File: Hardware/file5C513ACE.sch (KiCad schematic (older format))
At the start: 73 parts, among them J1 GATE_2, J2 GATE_3, J3 GATE_1, Q1 MMBT3904, Q2 MMBT3904, Q3 MMBT3904, SW1 Frequency Adjust, SW10 SET_SW, SW11 FILTER_SW, SW12 FILTEREXT_SW, SW13 SHAPE_SW, SW2 MOD_SW, SW3 FILTER1_SW, SW4 PROG, SW5 VOICE_SW, SW6 FILTER2_SW, SW7 RST, SW8 MODE_SW, SW9 FILTER3_SW, U1 TLC5947DAP

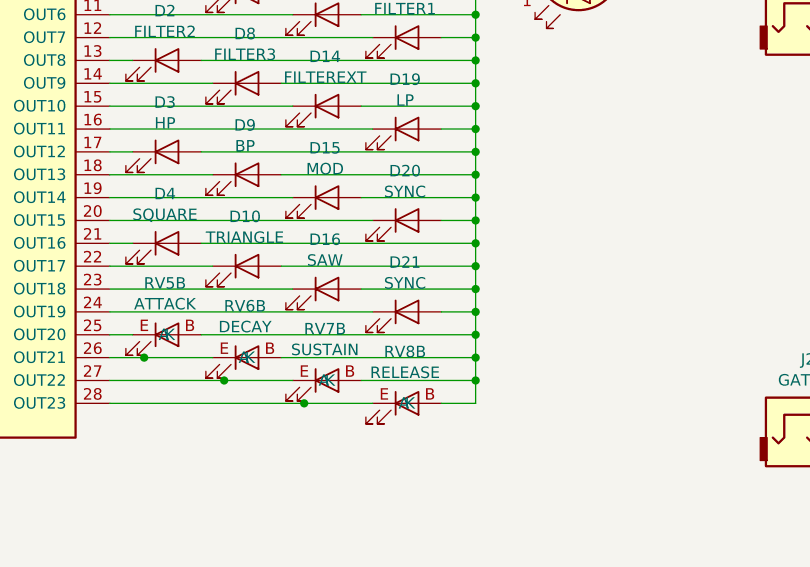
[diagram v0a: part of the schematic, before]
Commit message: Finished mechanical design on PCB
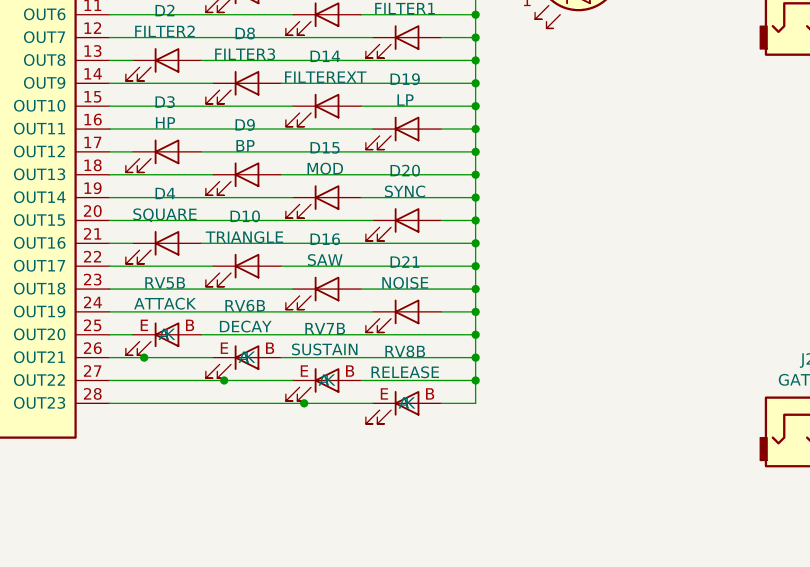
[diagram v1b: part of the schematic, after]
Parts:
- D21: value SYNC -> NOISE
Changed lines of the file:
@@
 AR Path="/5BFD63E3/5C513ACF/5C6023CE" Ref="D21"  Part="1"
 F 0 "D21" H 3791 5666 50  0000 C CNN
-F 1 "SYNC" H 3791 5575 50  0000 C CNN
+F 1 "NOISE" H 3791 5575 50  0000 C CNN
 F 2 "LED_THT:LED_D3.0mm" H 3800 5450 50  0001 C CNN
 F 3 "~" H 3800 5450 50  0001 C CNN

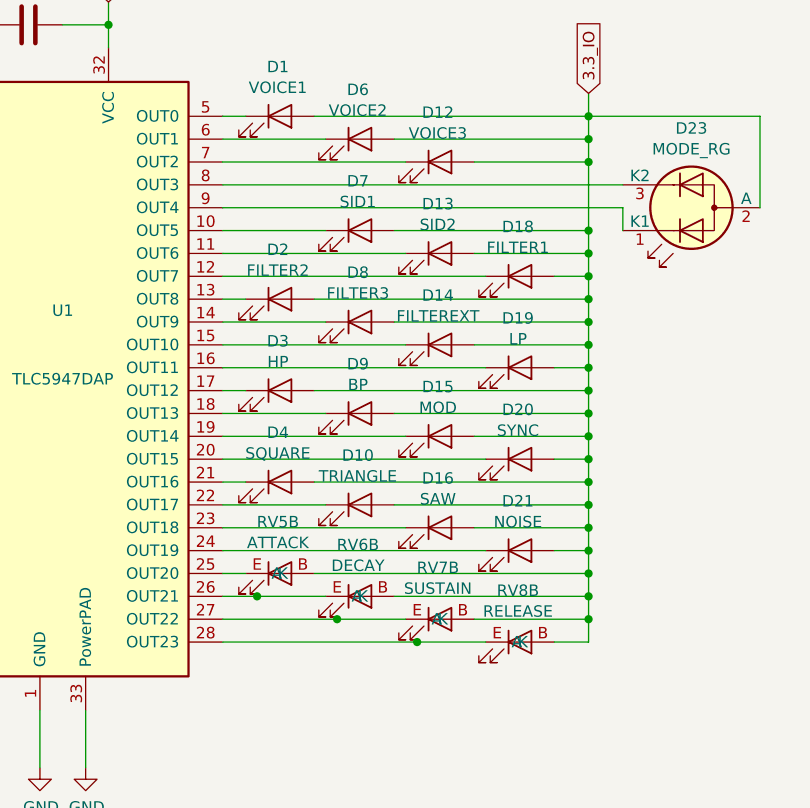
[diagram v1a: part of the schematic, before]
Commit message: Removed SID1 and SID2 led
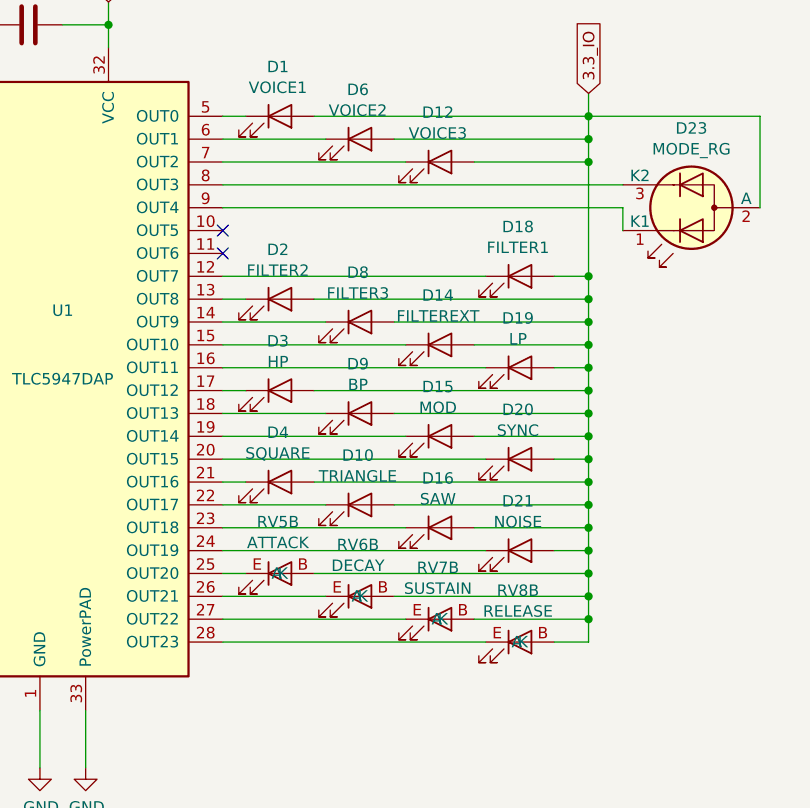
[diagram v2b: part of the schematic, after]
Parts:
- removed D13: SID2, LED_THT:LED_D3.0mm, symbol Device:LED
- removed D7: SID1, LED_THT:LED_D3.0mm, symbol Device:LED
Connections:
- no-connect marks 1 -> 3
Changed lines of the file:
@@
-$Comp
-L Device:LED D?
-U 1 1 5C602358
-P 3100 4050
-AR Path="/5BFD63E3/5C602358" Ref="D?"  Part="1"
-AR Path="/5BFD63E3/5C513ACF/5C602358" Ref="D7"  Part="1"
-F 0 "D7" H 3091 4266 50  0000 C CNN
-F 1 "SID1" H 3091 4175 50  0000 C CNN
-F 2 "LED_THT:LED_D3.0mm" H 3100 4050 50  0001 C CNN
-F 3 "~" H 3100 4050 50  0001 C CNN
-	1    3100 4050
-	1    0    0    -1
-$EndComp
-$Comp
-L Device:LED D?
-U 1 1 5C60235F
-P 3450 4150
-AR Path="/5BFD63E3/5C60235F" Ref="D?"  Part="1"
-AR Path="/5BFD63E3/5C513ACF/5C60235F" Ref="D13"  Part="1"
-F 0 "D13" H 3441 4366 50  0000 C CNN
-F 1 "SID2" H 3441 4275 50  0000 C CNN
-F 2 "LED_THT:LED_D3.0mm" H 3450 4150 50  0001 C CNN
-F 3 "~" H 3450 4150 50  0001 C CNN
-	1    3450 4150
-	1    0    0    -1
-$EndComp
 $Comp
 L Device:LED D?
@@
 	2500 3750 3300 3750
 Wire Wire Line
-	2500 4050 2950 4050
-Wire Wire Line
-	2500 4150 3300 4150
-Wire Wire Line
 	2500 4250 3650 4250
 Wire Wire Line
@@
 	2500 5550 2600 5550
 Wire Wire Line
-	2500 5650 2650 5650
-Wire Wire Line
-	2500 5750 3000 5750
-Wire Wire Line
-	2500 5850 3350 5850
-Wire Wire Line
 	4100 3450 4100 3550
 Wire Wire Line
@@
 Wire Wire Line
 	4100 4250 4100 4350
-Wire Wire Line
-	3600 4150 4100 4150
-Connection ~ 4100 4150
-Wire Wire Line
-	4100 4150 4100 4250
-Wire Wire Line
-	3250 4050 4100 4050
-Connection ~ 4100 4050
-Wire Wire Line
-	4100 4050 4100 4150
 Wire Wire Line
 	3600 3750 4100 3750
@@
 	700  4550 1100 4550
 NoConn ~ 1100 4950
-Wire Wire Line
-	4100 3750 4100 4050
 $Comp
 L Device:LED_Dual_CAC D23
@@
 	0    1    1    0
 $EndComp
-Connection ~ 2650 5650
-Wire Wire Line
-	2650 5650 2950 5650
-Connection ~ 3000 5750
-Wire Wire Line
-	3000 5750 3300 5750
-Connection ~ 3350 5850
-Wire Wire Line
-	3350 5850 3650 5850
+Wire Wire Line
+	2500 5650 2950 5650
+Wire Wire Line
+	2500 5750 3300 5750
+Wire Wire Line
+	2500 5850 3650 5850
+Wire Wire Line
+	4100 3750 4100 4250
+NoConn ~ 2500 4050
+NoConn ~ 2500 4150
 $EndSCHEMATC

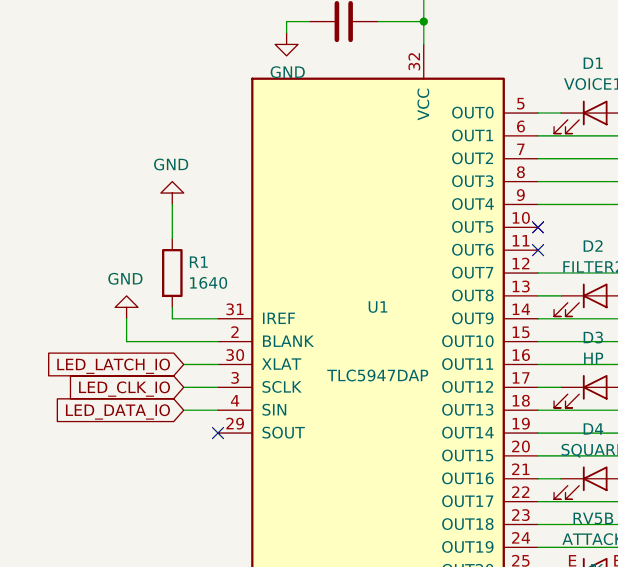
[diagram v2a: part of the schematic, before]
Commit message: STM32CubeMX Blinky
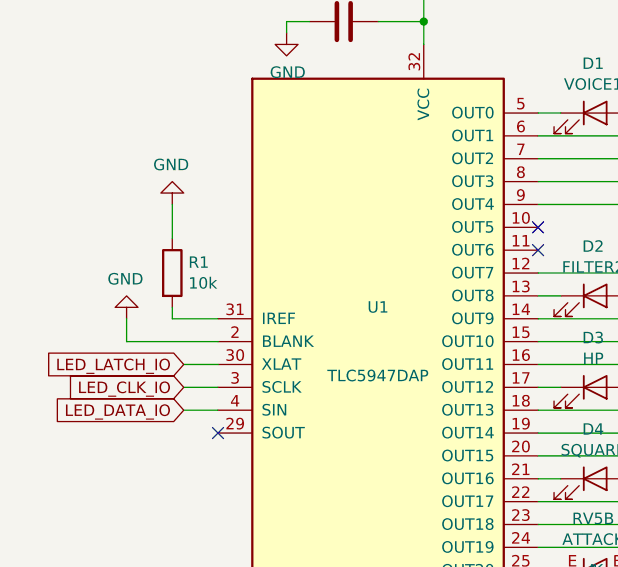
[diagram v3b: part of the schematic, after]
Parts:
- R1: value 1640 -> 10k
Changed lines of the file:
@@
 AR Path="/5BFD63E3/5C513ACF/5C602325" Ref="R1"  Part="1"
 F 0 "R1" H 970 4296 50  0000 L CNN
-F 1 "1640" H 970 4205 50  0000 L CNN
+F 1 "10k" H 970 4205 50  0000 L CNN
 F 2 "Resistor_SMD:R_0603_1608Metric" V 830 4250 50  0001 C CNN
 F 3 "~" H 900 4250 50  0001 C CNN

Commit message: IT WORKS
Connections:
- net 3.3_IO: now also C3.1, U1.32 (VCC); no longer D1.2 (A), D10.2 (A), D12.2 (A), D14.2 (A), D15.2 (A), D16.2 (A), D18.2 (A), D19.2 (A), D2.2 (A), D20.2 (A), D21.2 (A), D23.2 (A), D3.2 (A), D4.2 (A), D6.2 (A), D8.2 (A), D9.2 (A), RV5.B (A), RV6.B (A), RV7.B (A), RV8.B (A)
- net 5V_IO: now also D1.2 (A), D10.2 (A), D12.2 (A), D14.2 (A), D15.2 (A), D16.2 (A), D18.2 (A), D19.2 (A), D2.2 (A), D20.2 (A), D21.2 (A), D23.2 (A), D3.2 (A), D4.2 (A), D6.2 (A), D8.2 (A), D9.2 (A), RV5.B (A), RV6.B (A), RV7.B (A), RV8.B (A); no longer C3.1, U1.32 (VCC)
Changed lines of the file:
@@
 Text GLabel 1750 2500 3    50   Input ~ 0
 3.3_IO
-Text GLabel 2000 3050 1    50   Input ~ 0
+Text GLabel 4100 3450 1    50   Input ~ 0
 5V_IO
 Text GLabel 7250 800  1    50   Input ~ 0
@@
 	1    0    0    -1
 $EndComp
-Text GLabel 4100 3450 1    50   Input ~ 0
+Text GLabel 2000 3050 1    50   Input ~ 0
 3.3_IO
 $Comp

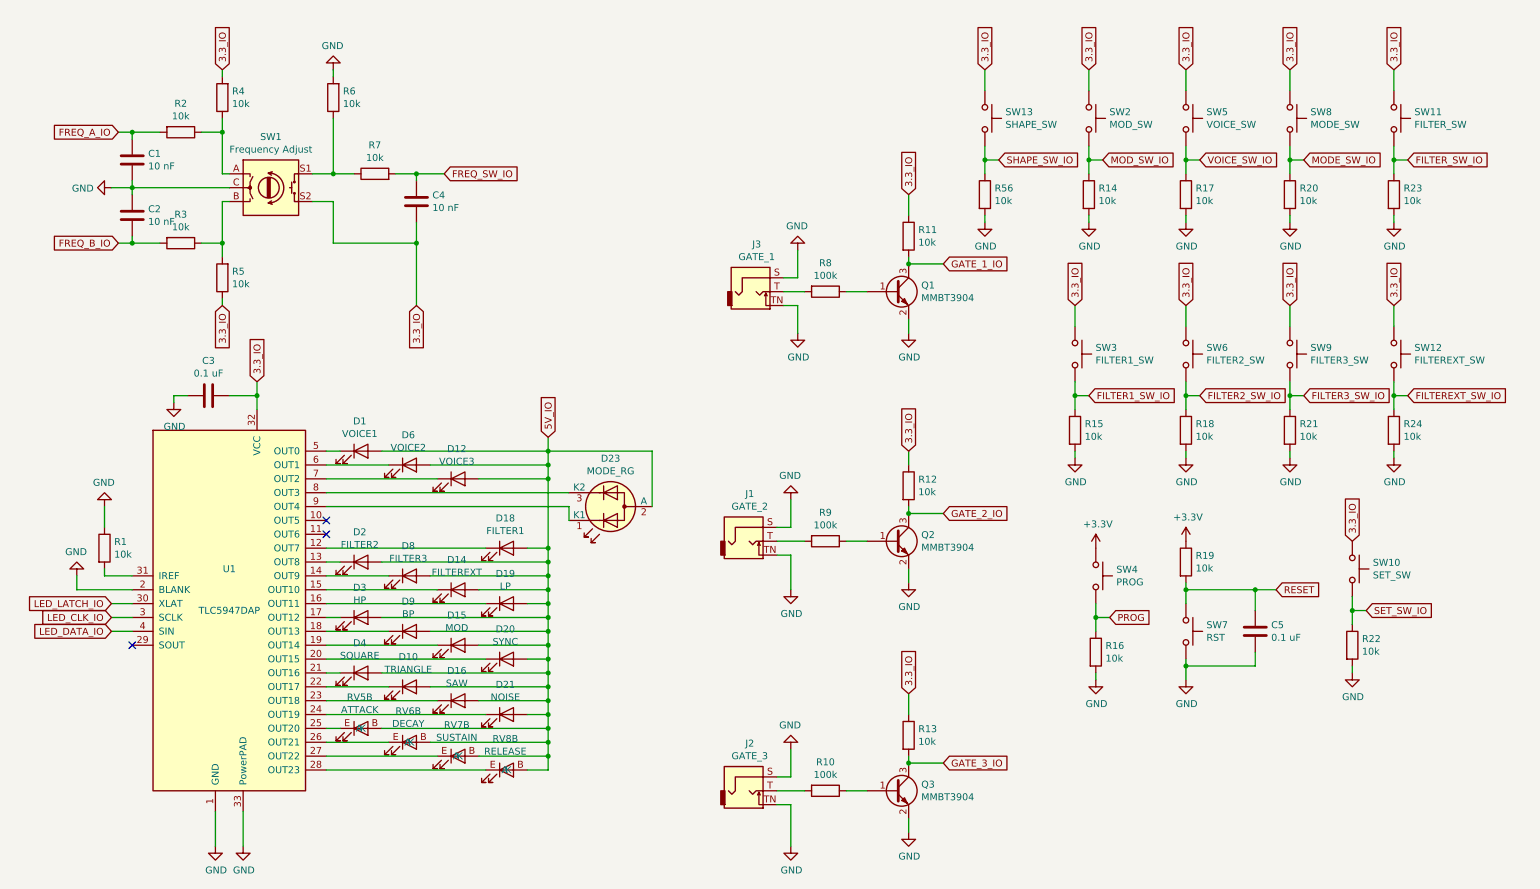
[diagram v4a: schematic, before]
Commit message: Updated to single four layer board
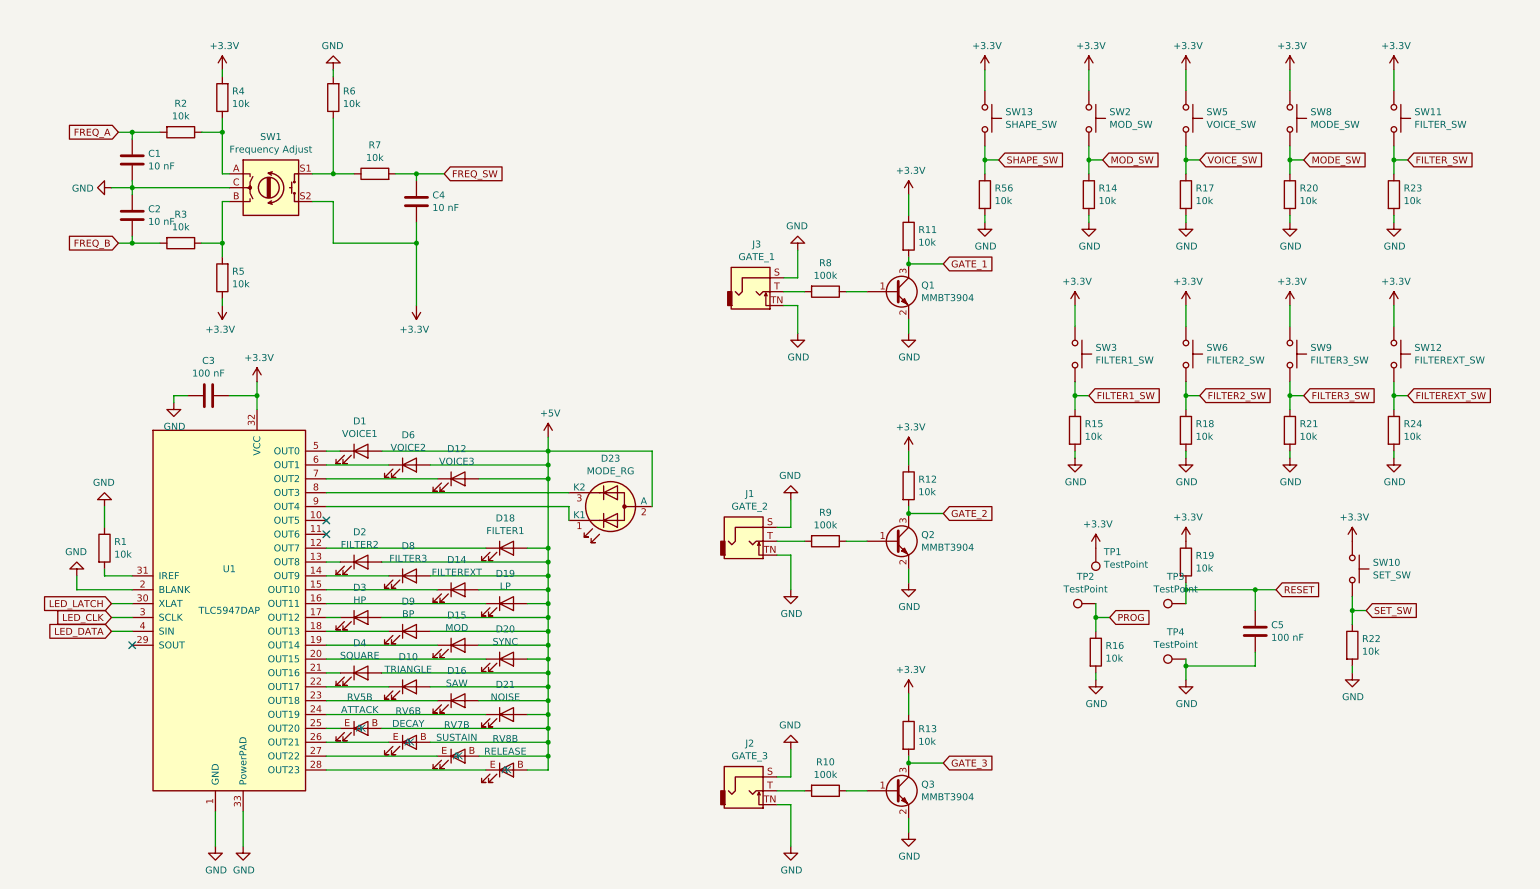
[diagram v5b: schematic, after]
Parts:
- removed SW4: PROG, Button_Switch_SMD:SW_SPST_EVPBF, symbol Switch:SW_Push
- removed SW7: RST, Button_Switch_SMD:SW_SPST_EVPBF, symbol Switch:SW_Push
- added TP1, TP2, TP3, TP4: TestPoint, TestPoint:TestPoint_Pad_D1.0mm, symbol Connector:TestPoint
- C3, C5: value 0.1 uF -> 100 nF
- D1, D10, D12, D14, D15, D16, D18, D19, D2, D20, D21, D3, D4, D6, D8, D9: footprint LED_THT:LED_D3.0mm -> LED_SMD:LED_0603_1608Metric
- D23: footprint LED_THT:LED_D3.0mm-3 -> LED_SMD:LED-L1T2_LUMILEDS
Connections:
- net 3.3_IO is gone; now on net +3V3: C3.1, C4.2, R11.1, R12.1, R13.1, R4.2, R5.1, SW1.S2, SW10.1, SW11.1, SW12.1, SW13.1, SW2.1, SW3.1, SW5.1, SW6.1, SW8.1, SW9.1, U1.32 (VCC)
- net +3V3: now also TP1.1
- net GND: now also TP4.1
- net PROG: now also TP2.1
- net RESET: now also TP3.1
- net 5V_IO renamed +5V
- net FILTER1_SW_IO renamed FILTER1_SW
- net FILTER2_SW_IO renamed FILTER2_SW
- net FILTER3_SW_IO renamed FILTER3_SW
- net FILTEREXT_SW_IO renamed FILTEREXT_SW
- net FILTER_SW_IO renamed FILTER_SW
- net FREQ_A_IO renamed FREQ_A
- net FREQ_B_IO renamed FREQ_B
- net FREQ_SW_IO renamed FREQ_SW
- net GATE_1_IO renamed GATE_1
- net GATE_2_IO renamed GATE_2
- net GATE_3_IO renamed GATE_3
- net LED_CLK_IO renamed LED_CLK
- net LED_DATA_IO renamed LED_DATA
- net LED_LATCH_IO renamed LED_LATCH
- net MODE_SW_IO renamed MODE_SW
- net MOD_SW_IO renamed MOD_SW
- net SET_SW_IO renamed SET_SW
- net SHAPE_SW_IO renamed SHAPE_SW
- net VOICE_SW_IO renamed VOICE_SW

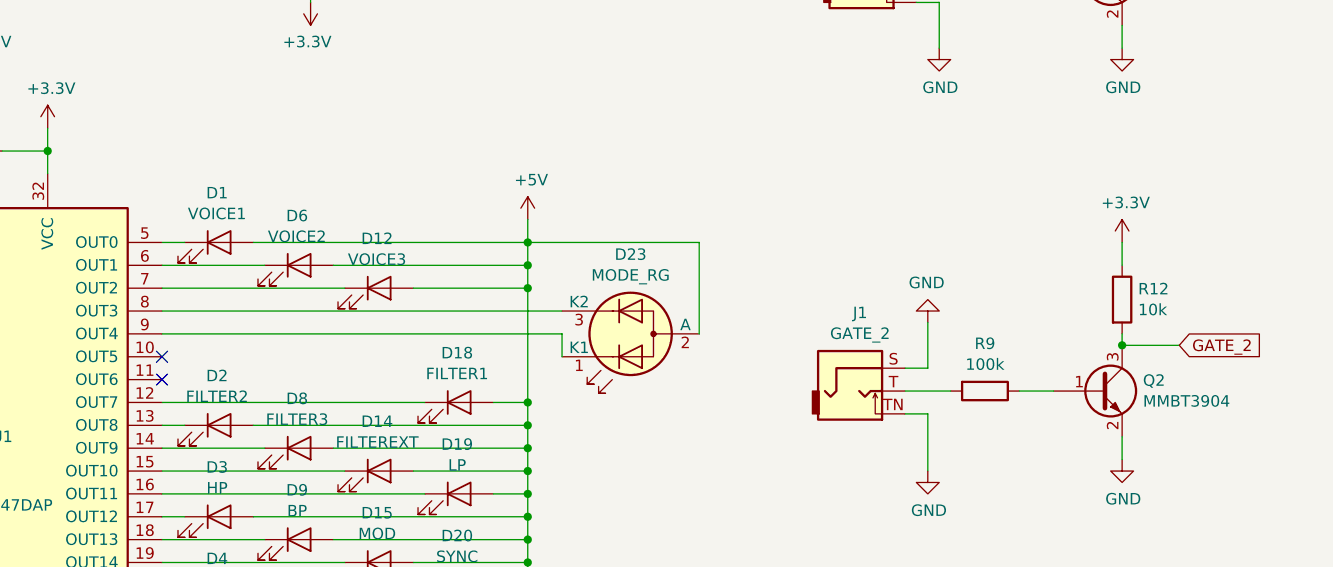
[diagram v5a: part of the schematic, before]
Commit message: Finished design of 4 layer, added stero option and logo
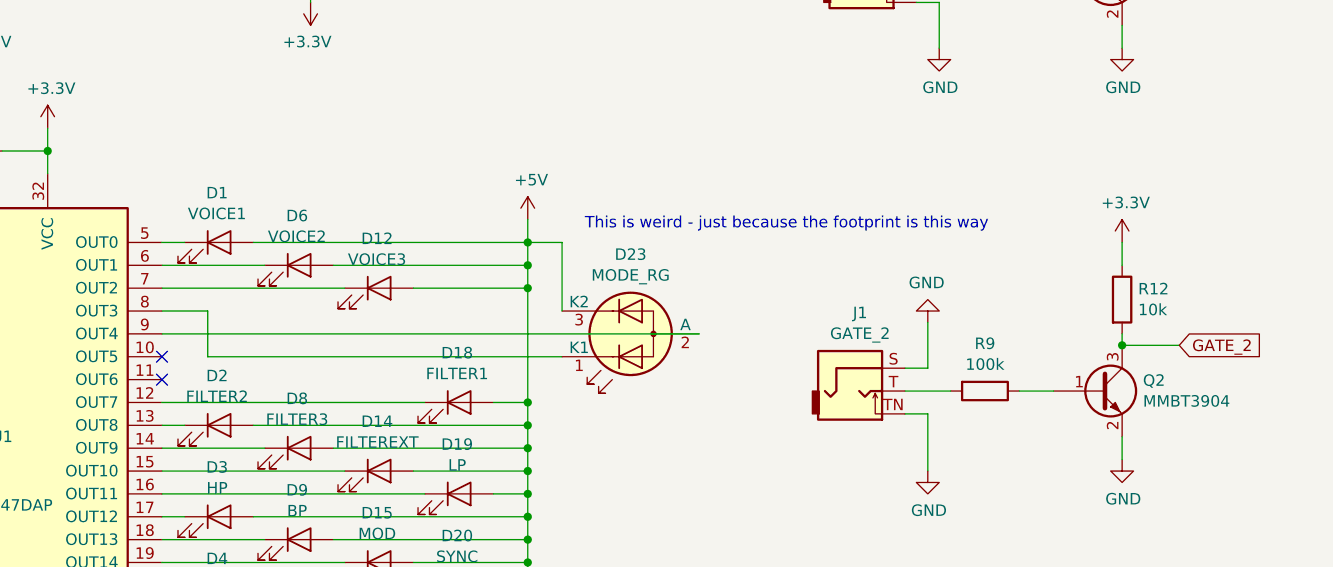
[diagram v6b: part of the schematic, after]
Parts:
- D23: footprint LED_SMD:LED-L1T2_LUMILEDS -> Package_TO_SOT_SMD:SOT-23
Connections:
- net +5V: now also D23.3 (K2); no longer D23.2 (A)
- net at D23.1 (K1): now also U1.8 (OUT3); no longer U1.9 (OUT4)
- new net: D23.2 (A), U1.9 (OUT4)
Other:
- note added: "This is weird - just because the footprint is this way"
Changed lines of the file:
@@
 F 0 "D23" H 4550 3603 50  0000 C CNN
 F 1 "MODE_RG" H 4550 3694 50  0000 C CNN
-F 2 "LED_SMD:LED-L1T2_LUMILEDS" H 4600 3950 50  0001 C CNN
+F 2 "Package_TO_SOT_SMD:SOT-23" H 4600 3950 50  0001 C CNN
 F 3 "~" H 4600 3950 50  0001 C CNN
 	1    4550 3950
 	-1   0    0    1
 $EndComp
-Wire Wire Line
-	2500 3850 4250 3850
-Wire Wire Line
-	4250 4050 4250 3950
-Wire Wire Line
-	2500 3950 4250 3950
-Wire Wire Line
-	4850 3950 4850 3550
-Wire Wire Line
-	4850 3550 4100 3550
 $Comp
 L Switch:SW_Push SW?
@@
 	0    -1   -1   0
 $EndComp
+Wire Wire Line
+	4850 3950 2500 3950
+Wire Wire Line
+	4250 4050 2700 4050
+Wire Wire Line
+	2700 4050 2700 3850
+Wire Wire Line
+	2700 3850 2500 3850
+Wire Wire Line
+	4250 3850 4250 3550
+Wire Wire Line
+	4250 3550 4100 3550
+Text Notes 4350 3500 0    50   ~ 0
+This is weird - just because the footprint is this way
 $EndSCHEMATC
